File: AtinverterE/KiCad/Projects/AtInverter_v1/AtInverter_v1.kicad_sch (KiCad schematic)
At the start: 60 parts

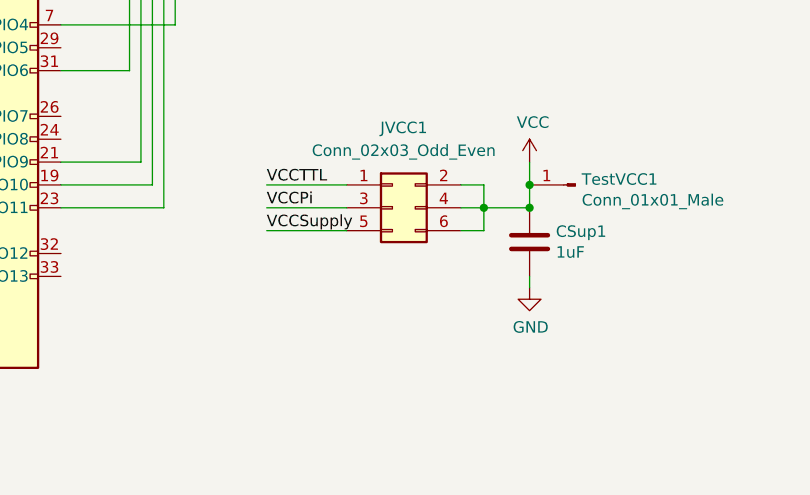
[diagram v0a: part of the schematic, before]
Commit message: Changed footprint for IR2302 to SMD
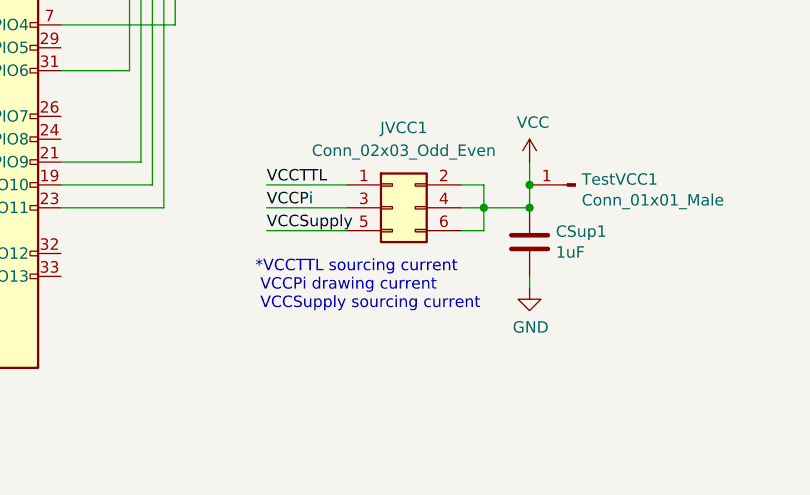
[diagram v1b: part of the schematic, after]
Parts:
- GateDriver1, GateDriver2: footprint Package_DIP:DIP-8_W7.62mm_LongPads -> Atinverter_vE:PG-DSO-8-910_INF
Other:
- note added: "*VCCTTL sourcing current VCCPi drawing current VCCSupply sourcing current"
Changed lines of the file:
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@@
+    (effects (font (size 1.27 1.27)) (justify left bottom))
+  )
+  (text "*VCCTTL sourcing current\n VCCPi drawing current\n VCCSupply sourcing current\n"
+    (at 77.47 175.26 0)
     (effects (font (size 1.27 1.27)) (justify left bottom))
   )
@@
       (effects (font (size 1.27 1.27)))
     )
-    (property "Footprint" "Package_DIP:DIP-8_W7.62mm_LongPads" (at 105.41 59.9694 0)
+    (property "Footprint" "Atinverter_vE:PG-DSO-8-910_INF" (at 105.41 59.9694 0)
       (effects (font (size 1.27 1.27) italic) hide)
     )
@@
       (effects (font (size 1.27 1.27)))
     )
-    (property "Footprint" "Package_DIP:DIP-8_W7.62mm_LongPads" (at 170.18 59.9694 0)
+    (property "Footprint" "Atinverter_vE:PG-DSO-8-910_INF" (at 170.18 59.9694 0)
       (effects (font (size 1.27 1.27) italic) hide)
     )
